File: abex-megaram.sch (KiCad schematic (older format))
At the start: 13 parts, among them P1 0877159106, P2 CONN_01X01, P3 CONN_01X01, P4 CONN_01X01, P5 CONN_01X01, P6 CONN_01X01, SW2 SW_Push

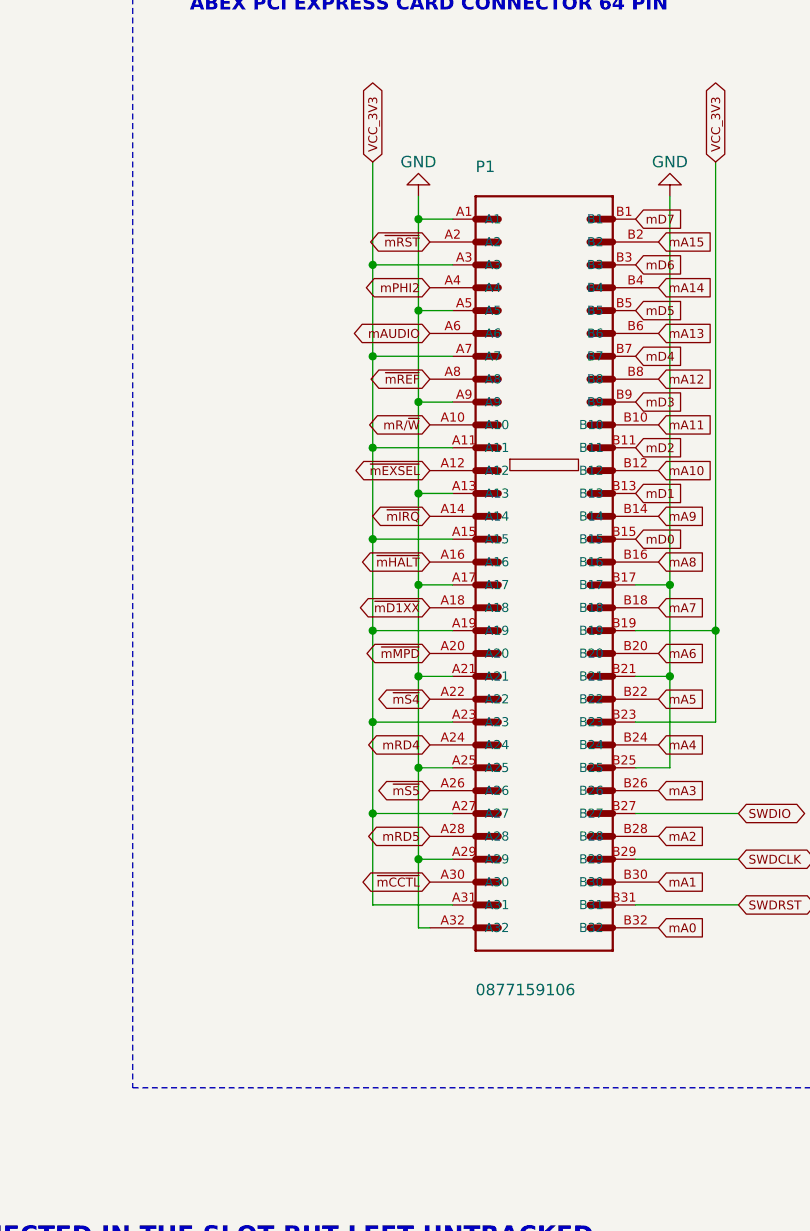
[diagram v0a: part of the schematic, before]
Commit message: Optimized for 8 bit access. Added a configuration option. A31 on connector is 5VDC. Not used here
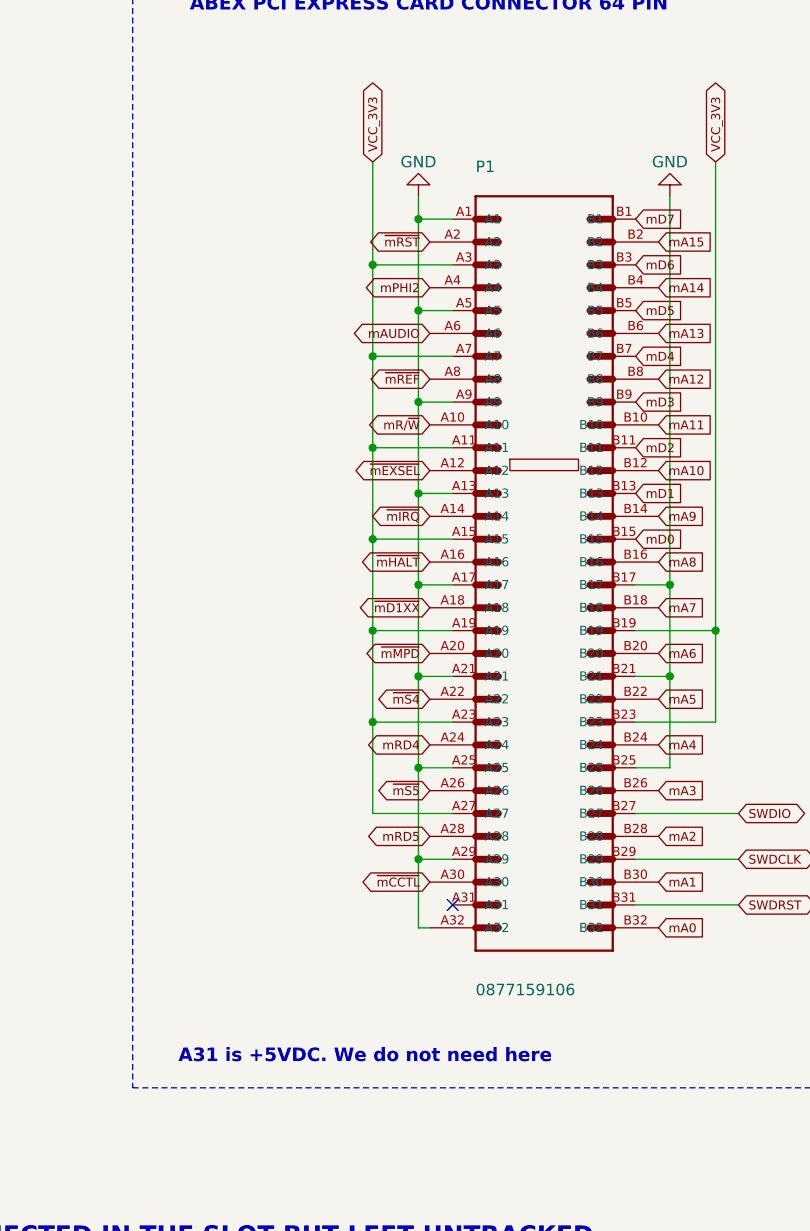
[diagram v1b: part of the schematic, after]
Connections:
- net VCC: no longer P1.A31
- no-connect marks 8 -> 9
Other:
- note added: "A31 is +5VDC. We do not need here"
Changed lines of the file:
@@
 LIBS:Amplifier_Instrumentation
 LIBS:Amplifier_Buffer
-LIBS:ft232rl
 LIBS:AmigaComponents
 LIBS:abex-megaram-cache
@@
 VCC_3V3
 Wire Wire Line
-	4850 2100 4850 5350
-Wire Wire Line
 	4850 2550 5200 2550
 Wire Wire Line
@@
 	4850 4950 5200 4950
 Connection ~ 4850 4550
-Wire Wire Line
-	4850 5350 5200 5350
-Connection ~ 4850 4950
 Wire Wire Line
 	6000 4550 6350 4550
@@
 Text Notes 4050 1450 0    60   ~ 12
 ABEX PCI EXPRESS CARD CONNECTOR 64 PIN
+Wire Wire Line
+	4850 4950 4850 2100
+NoConn ~ 5200 5350
+Text Notes 4000 6050 0    59   ~ 12
+A31 is +5VDC. We do not need here
 $EndSCHEMATC

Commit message: New layout and design
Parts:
- removed P6: CONN_01X01, Measurement_Points:Measurement_Point_Round-SMD-Pad_Small, symbol CONN_01X01
- renumbered C30 to C1, R6 to R1, R1 to R2, SW2 to SW1
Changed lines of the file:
@@
 $EndComp
-$Comp
-L CONN_01X01 P6
-U 1 1 5C2B6F21
-P 8550 4800
-F 0 "P6" H 8550 4900 50  0000 C CNN
-F 1 "CONN_01X01" H 8500 4650 50  0000 C CNN
-F 2 "Measurement_Points:Measurement_Point_Round-SMD-Pad_Small" H 8550 4800 50  0001 C CNN
-F 3 "" H 8550 4800 60  0001 C CNN
-	1    8550 4800
-	-1   0    0    1
-$EndComp
-Text GLabel 8750 4800 2    60   Output ~ 0
-TP1
 $Comp
 L CONN_01X01 P2
@@
 $EndComp
 $Comp
-L R_Small R6
+L R_Small R1
 U 1 1 5CA86A49
 P 1800 5700
-F 0 "R6" H 1830 5720 50  0000 L CNN
+F 0 "R1" H 1830 5720 50  0000 L CNN
 F 1 "100K" H 1830 5660 50  0000 L CNN
 F 2 "Resistors_SMD:R_1206_HandSoldering" H 1800 5700 50  0001 C CNN
@@
 $EndComp
 $Comp
-L SW_Push SW2
+L SW_Push SW1
 U 1 1 5CA86A5D
 P 1800 5200
-F 0 "SW2" H 1850 5300 50  0000 L CNN
+F 0 "SW1" H 1850 5300 50  0000 L CNN
 F 1 "SW_Push" H 1800 5140 50  0000 C CNN
 F 2 "RetroBitLab:SW_SPST_FSMSM_3D" H 1800 5400 50  0001 C CNN
@@
 $EndSheet
 $Comp
-L C_Small C30
+L C_Small C1
 U 1 1 5CBFBE9A
 P 2100 5200
-F 0 "C30" H 2110 5270 50  0000 L CNN
+F 0 "C1" H 2110 5270 50  0000 L CNN
 F 1 "100n" H 2110 5120 50  0000 L CNN
 F 2 "Capacitors_SMD:C_1206_HandSoldering" H 2100 5200 50  0001 C CNN
@@
 	10200 3250 10350 3250
 $Comp
-L R_Small R1
+L R_Small R2
 U 1 1 5CC44929
 P 10450 3250
-F 0 "R1" V 10550 3300 50  0000 L CNN
+F 0 "R2" V 10550 3300 50  0000 L CNN
 F 1 "0" V 10550 3200 50  0000 L CNN
 F 2 "Resistors_SMD:R_1206_HandSoldering" H 10450 3250 50  0001 C CNN
